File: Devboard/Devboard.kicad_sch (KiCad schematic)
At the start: 32 parts, among them J1 USB_C_Receptacle_USB2.0_14P, J2 Conn_01x20, J3 Conn_01x20, SW1 SW_Push, U1 RP2040, U2 MCP1700x-120xxMB, U3 W25Q128JVS, Y2 Crystal_GND24

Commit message: Worked on adding batteries and an oled screen.
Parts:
- added J4: Conn_01x03, Connector_PinHeader_1.00mm:PinHeader_1x03_P1.00mm_Vertical, symbol Connector_Generic:Conn_01x03
- added SW2: SW_Push, Button_Switch_SMD:SW_SPST_TS-1088-xR020, symbol Switch:SW_Push
- added U4: ER_OLEDM0.91_1x-I2C, Display:ER_OLEDM0.91_1x-I2C, symbol Display_Graphic:ER_OLEDM0.91_1x-I2C
- added XT1: (no value), JST-PH-2.:JST-PH-2, symbol New_Library:XT30
- C1, C10, C11, C12, C13, C14, C17, C2, C3, C4, C5, C6, C7, C8, C9: footprint (none) -> Capacitor_SMD:C_0201_0603Metric_Pad0.64x0.40mm_HandSolder
- C15, C16: value 15pf -> 33uf; footprint (none) -> Capacitor_SMD:C_0201_0603Metric_Pad0.64x0.40mm_HandSolder
- J1: footprint (none) -> Connector_USB:USB_C_Receptacle_HRO_TYPE-C-31-M-17
- J2, J3: footprint (none) -> Connector_PinHeader_1.00mm:PinHeader_1x20_P1.00mm_Vertical
- R1, R2, R3, R4, R5, R6, R7: footprint (none) -> Resistor_SMD:R_0402_1005Metric_Pad0.72x0.64mm_HandSolder
- SW1: footprint (none) -> Button_Switch_SMD:SW_SPST_TS-1088-xR020
- Y2: footprint (none) -> Crystal:Crystal_SMD_3225-4Pin_3.2x2.5mm_HandSoldering
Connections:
- net +3V3: now also J3.5 (Pin_5), XT1.1 (Power); no longer J3.15 (Pin_15)
- net GND: now also U1.8 (GPIO6), J4.2 (Pin_2), SW2.2, U4.1 (GND), XT1.2 (GND)
- net GPIO16: now also J3.20 (Pin_20)
- net GPIO17: now also J3.19 (Pin_19)
- net GPIO18: now also J3.17 (Pin_17)
- net GPIO19: now also J3.16 (Pin_16)
- net GPIO20: now also J3.15 (Pin_15)
- net GPIO21: now also J3.14 (Pin_14)
- net GPIO22: now also SW2.1
- net GPIO23: now also U4.3 (SCL)
- net GPIO24: now also U4.4 (SDA)
- net GPIO26: now also J3.7 (Pin_7)
- net GPIO27: now also J3.6 (Pin_6)
- net GPIO28: now also J3.4 (Pin_4)
- net GPIO29: now also J3.2 (Pin_2)
- net VBUS: now also J3.1 (Pin_1), U4.2 (VCC); no longer J3.20 (Pin_20)
- net RUN: now reaches J3.11 (Pin_11)
- net SWCLK: now reaches U1.24 (SWCLK)
- net SWCLK: now also J4.1 (Pin_1)
- net SWD: now reaches U1.25 (SWDIO)
- net SWD: now also J4.3 (Pin_3)
- net GPIO6: no longer names the net of J2.9 (Pin_9)
- net GPIO6: no longer U1.8 (GPIO6)
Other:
- note added: "Break out pins"
- note added: "Crystal"
- note added: "Extras"
- note added: "For programable input"
- note added: "RP2040 and Decoupling Caps"
- note added: "This is for the Lipo Battery"
- note added: "USB C"
- note added: "https://www.racedayquads.com/products/newbeedrone-nitro-nectar-gold-3-8v-1s-300mah-30-60c-lihv-whoop-micro-battery-ph2-0-plastic-head?keyword=1s%203v%20"
- note added: "oled screen"
- moved on the sheet: C1, C10, C11, C12, C13, C14, C15, C16, C17, C2, C3, C4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

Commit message: Worked on routing
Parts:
- J1: footprint Connector_USB:USB_C_Receptacle_HRO_TYPE-C-31-M-17 -> Connector_USB:USB_C_Receptacle_HRO_TYPE-C-31-M-12
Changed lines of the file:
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@@
 			)
 		)
-		(property "Footprint" "Connector_USB:USB_C_Receptacle_HRO_TYPE-C-31-M-17"
+		(property "Footprint" "Connector_USB:USB_C_Receptacle_HRO_TYPE-C-31-M-12"
 			(at 48.26 54.61 0)
 			(hide yes)

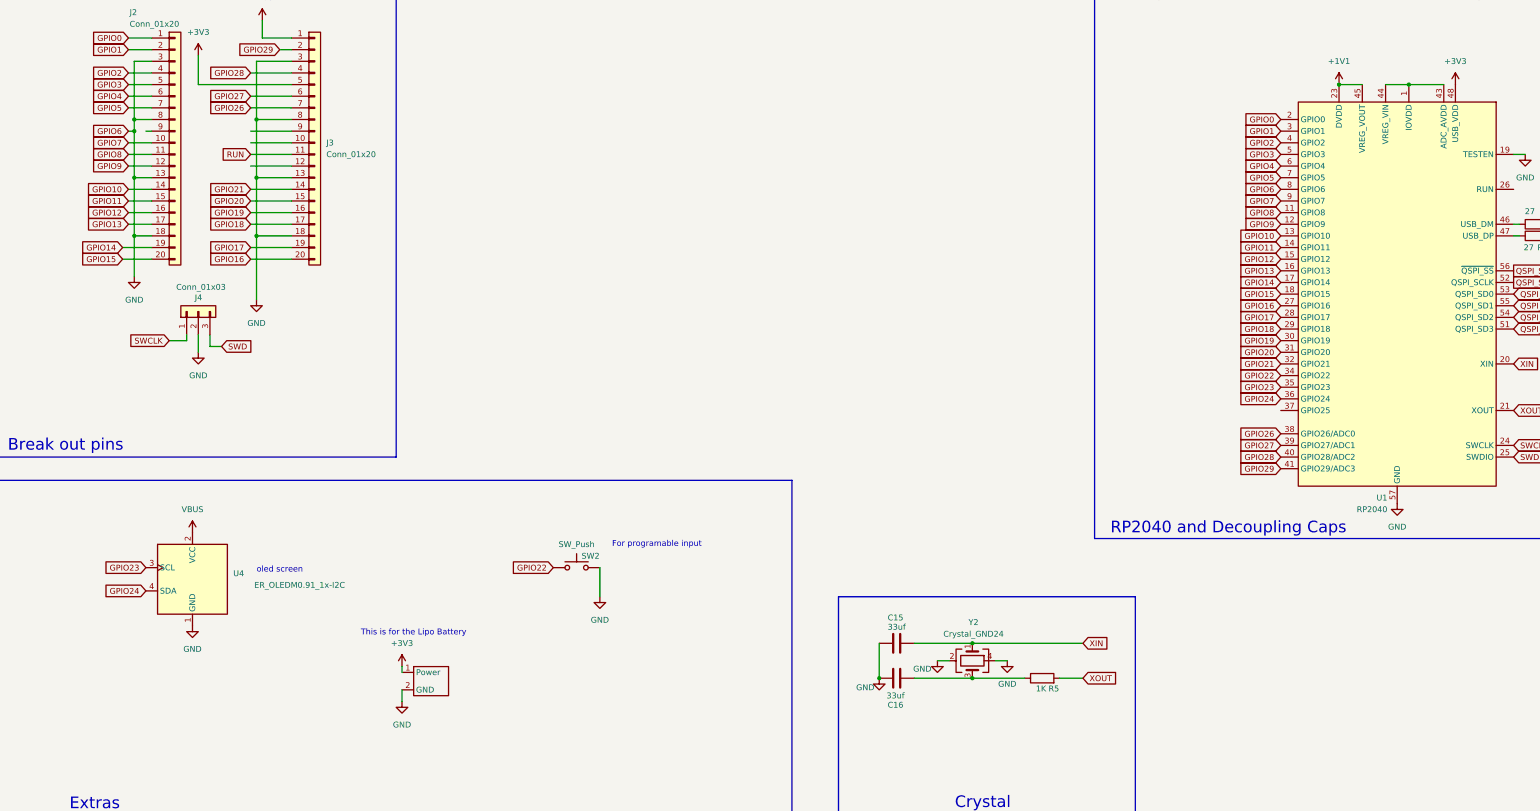
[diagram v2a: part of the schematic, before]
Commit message: Routed the pins more.
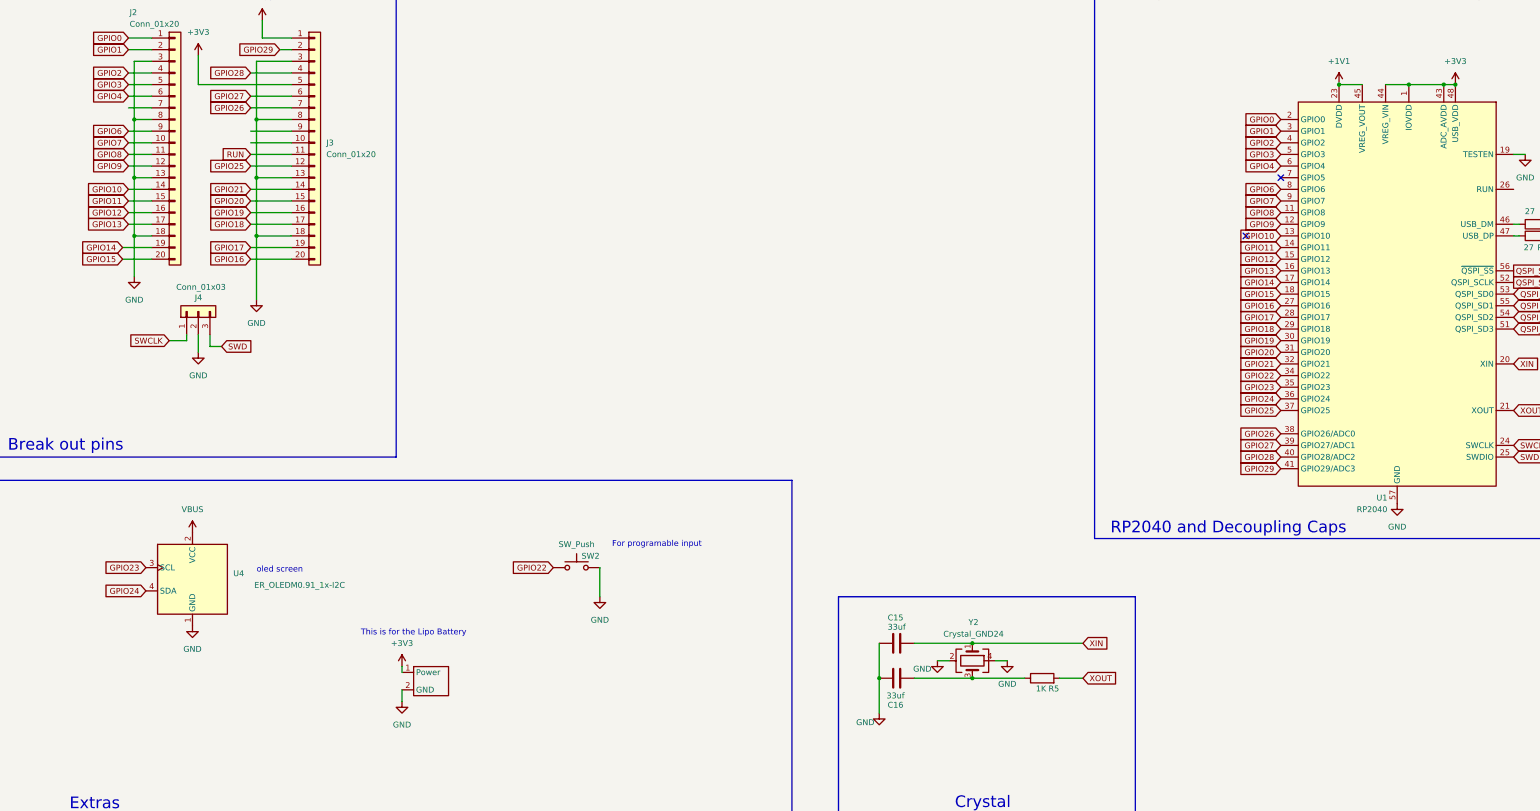
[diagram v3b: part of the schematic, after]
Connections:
- net +3V3: now also U1.1 (IOVDD), U1.10 (IOVDD), U1.22 (IOVDD), U1.33 (IOVDD), U1.42 (IOVDD), U1.43 (ADC_AVDD), U1.44 (VREG_VIN), U1.49 (IOVDD)
- net GND: no longer U1.8 (GPIO6)
- net GPIO6: now reaches J2.9 (Pin_9)
- net GPIO6: now also U1.8 (GPIO6)
- net GPIO25: now reaches J3.12 (Pin_12)
- net GPIO25: now also U1.37 (GPIO25)
- net GPIO5: no longer names the net of J2.7 (Pin_7)
- net GPIO5: no longer U1.7 (GPIO5)
- no-connect marks 0 -> 2
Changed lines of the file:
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@@
 	)
 	(junction
-		(at 209.55 254)
-		(diameter 0)
-		(color 0 0 0 0)
-	)
-	(junction
 		(at 73.66 132.08)
 		(diameter 0)
@@
 	)
 	(junction
+		(at 332.74 124.46)
+		(diameter 0)
+		(color 0 0 0 0)
+	)
+	(junction
 		(at 341.63 100.33)
 		(diameter 0)
@@
 	)
 	(junction
+		(at 335.28 124.46)
+		(diameter 0)
+		(color 0 0 0 0)
+	)
+	(junction
 		(at 363.22 41.91)
 		(diameter 0)
@@
 	)
 	(junction
-		(at 271.78 92.71)
+		(at 209.55 254)
 		(diameter 0)
 		(color 0 0 0 0)
 	)
 	(junction
-		(at 46.99 144.78)
+		(at 271.78 92.71)
 		(diameter 0)
 		(color 0 0 0 0)
 	)
 	(junction
-		(at 46.99 134.62)
+		(at 46.99 144.78)
 		(diameter 0)
 		(color 0 0 0 0)
@@
 		(color 0 0 0 0)
 	)
+	(no_connect
+		(at 297.18 144.78)
+	)
+	(no_connect
+		(at 289.56 157.48)
+	)
 	(wire
 		(pts
@@
 	(wire
 		(pts
+			(xy 332.74 124.46) (xy 335.28 124.46)
+		)
+		(stroke
+			(width 0)
+			(type default)
+		)
+	)
+	(wire
+		(pts
 			(xy 59.69 57.15) (xy 59.69 59.69)
 		)
@@
 	(wire
 		(pts
-			(xy 45.72 134.62) (xy 46.99 134.62)
-		)
-		(stroke
-			(width 0)
-			(type default)
-		)
-	)
-	(wire
-		(pts
-			(xy 49.53 134.62) (xy 50.8 134.62)
+			(xy 45.72 134.62) (xy 50.8 134.62)
 		)
 		(stroke
@@
 	(wire
 		(pts
-			(xy 46.99 134.62) (xy 46.99 144.78)
+			(xy 46.99 132.08) (xy 46.99 144.78)
 		)
 		(stroke
@@
 	(wire
 		(pts
+			(xy 209.55 261.62) (xy 209.55 254)
+		)
+		(stroke
+			(width 0)
+			(type default)
+		)
+	)
+	(wire
+		(pts
 			(xy 45.72 137.16) (xy 50.8 137.16)
 		)
@@
 	(wire
 		(pts
-			(xy 46.99 132.08) (xy 46.99 134.62)
-		)
-		(stroke
-			(width 0)
-			(type default)
-		)
-	)
-	(wire
-		(pts
 			(xy 72.39 147.32) (xy 81.28 147.32)
 		)
@@
 		)
 	)
+	(global_label "GPIO25"
+		(shape input)
+		(at 297.18 195.58 180)
+		(fields_autoplaced yes)
+		(effects
+			(font
+				(size 1.27 1.27)
+			)
+			(justify right)
+		)
+		(property "Intersheetrefs" "${INTERSHEET_REFS}"
+			(at 287.3005 195.58 0)
+			(hide yes)
+			(show_name no)
+			(do_not_autoplace no)
+			(effects
+				(font
+					(size 1.27 1.27)
+				)
+				(justify right)
+			)
+		)
+	)
 	(global_label "QSPI_SS"
 		(shape output)
@@
 		)
 	)
-	(global_label "GPIO5"
-		(shape input)
-		(at 297.18 144.78 180)
-		(fields_autoplaced yes)
-		(effects
-			(font
-				(size 1.27 1.27)
-			)
-			(justify right)
-		)
-		(property "Intersheetrefs" "${INTERSHEET_REFS}"
-			(at 288.51 144.78 0)
-			(hide yes)
-			(show_name no)
-			(do_not_autoplace no)
-			(effects
-				(font
-					(size 1.27 1.27)
-				)
-				(justify right)
-			)
-		)
-	)
 	(global_label "SWD"
 		(shape input)
@@
 		)
 	)
-	(global_label "GPIO5"
-		(shape input)
-		(at 45.72 129.54 180)
-		(fields_autoplaced yes)
-		(effects
-			(font
-				(size 1.27 1.27)
-			)
-			(justify right)
-		)
-		(property "Intersheetrefs" "${INTERSHEET_REFS}"
-			(at 37.05 129.54 0)
-			(hide yes)
-			(show_name no)
-			(do_not_autoplace no)
-			(effects
-				(font
-					(size 1.27 1.27)
-				)
-				(justify right)
-			)
-		)
-	)
 	(global_label "GPIO29"
 		(shape input)
@@
 		)
 	)
+	(global_label "GPIO25"
+		(shape input)
+		(at 72.39 142.24 180)
+		(fields_autoplaced yes)
+		(effects
+			(font
+				(size 1.27 1.27)
+			)
+			(justify right)
+		)
+		(property "Intersheetrefs" "${INTERSHEET_REFS}"
+			(at 62.5105 142.24 0)
+			(hide yes)
+			(show_name no)
+			(do_not_autoplace no)
+			(effects
+				(font
+					(size 1.27 1.27)
+				)
+				(justify right)
+			)
+		)
+	)
 	(global_label "GPIO10"
 		(shape input)
@@
 	(symbol
 		(lib_id "power:GND")
-		(at 209.55 254 0)
+		(at 209.55 261.62 0)
 		(unit 1)
 		(body_style 1)
@@
 		(dnp no)
 		(property "Reference" "#PWR014"
-			(at 209.55 260.35 0)
+			(at 209.55 267.97 0)
 			(hide yes)
 			(show_name no)
@@
 		)
 		(property "Value" "GND"
-			(at 206.502 256.032 0)
+			(at 206.502 263.652 0)
 			(show_name no)
 			(do_not_autoplace no)
@@
 		)
 		(property "Footprint" ""
-			(at 209.55 254 0)
+			(at 209.55 261.62 0)
 			(hide yes)
 			(show_name no)
@@
 		)
 		(property "Datasheet" ""
-			(at 209.55 254 0)
+			(at 209.55 261.62 0)
 			(hide yes)
 			(show_name no)
@@
 		)
 		(property "Description" "Power symbol creates a global label with name \"GND\" , ground"
-			(at 209.55 254 0)
+			(at 209.55 261.62 0)
 			(hide yes)
 			(show_name no)

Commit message: Routing part 2 electric boogalooo
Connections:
- no-connect marks 2 -> 1
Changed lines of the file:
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@@
 		(at 297.18 144.78)
-	)
-	(no_connect
-		(at 289.56 157.48)
 	)
 	(wire
